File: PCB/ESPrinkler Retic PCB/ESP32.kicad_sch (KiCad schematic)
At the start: 2 parts, among them J3 Conn_01x19, J4 Conn_01x19

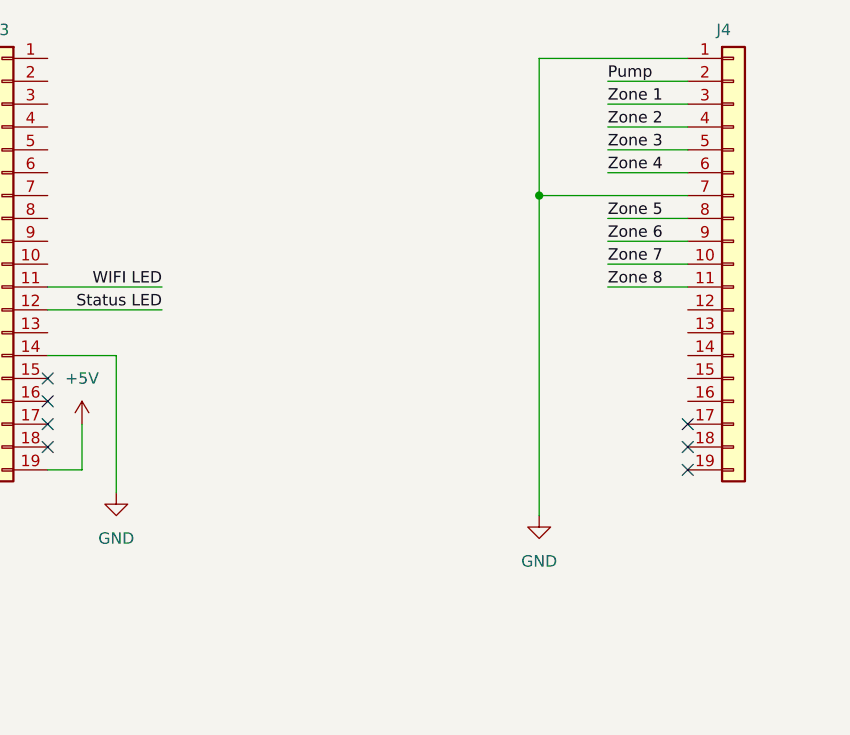
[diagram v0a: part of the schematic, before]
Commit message: Continue migrating PCB project to multi sheet design
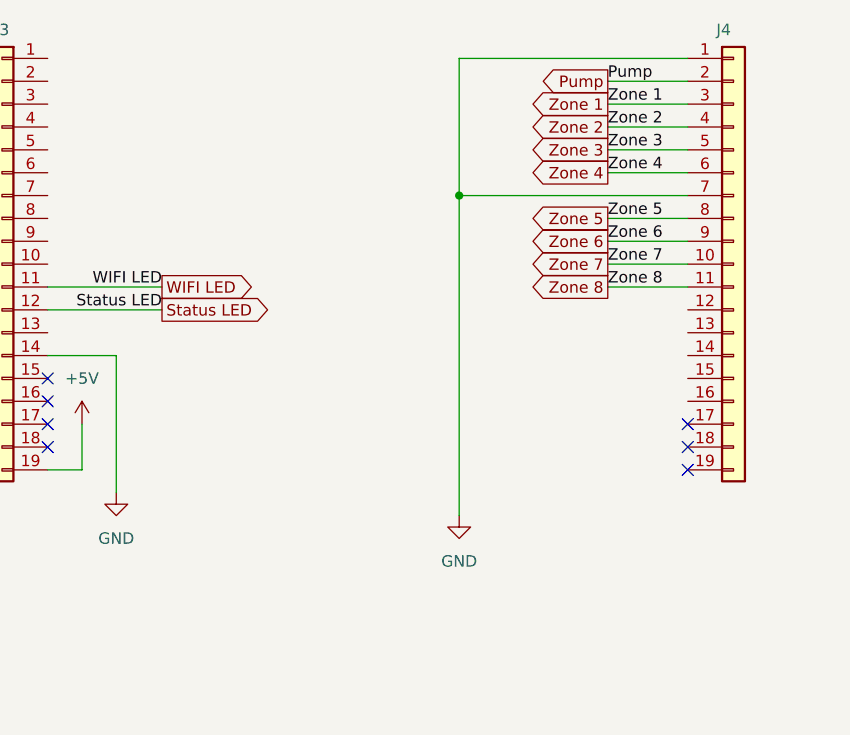
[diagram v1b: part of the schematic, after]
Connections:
- net Pump CTRL renamed Pump
- net Status LED CTRL renamed Status LED
- net WIFI LED CTRL renamed WIFI LED
- net Zone 1 CTRL renamed Zone 1
- net Zone 2 CTRL renamed Zone 2
- net Zone 3 CTRL renamed Zone 3
- net Zone 4 CTRL renamed Zone 4
- net Zone 5 CTRL renamed Zone 5
- net Zone 6 CTRL renamed Zone 6
- net Zone 7 CTRL renamed Zone 7
- net Zone 8 CTRL renamed Zone 8

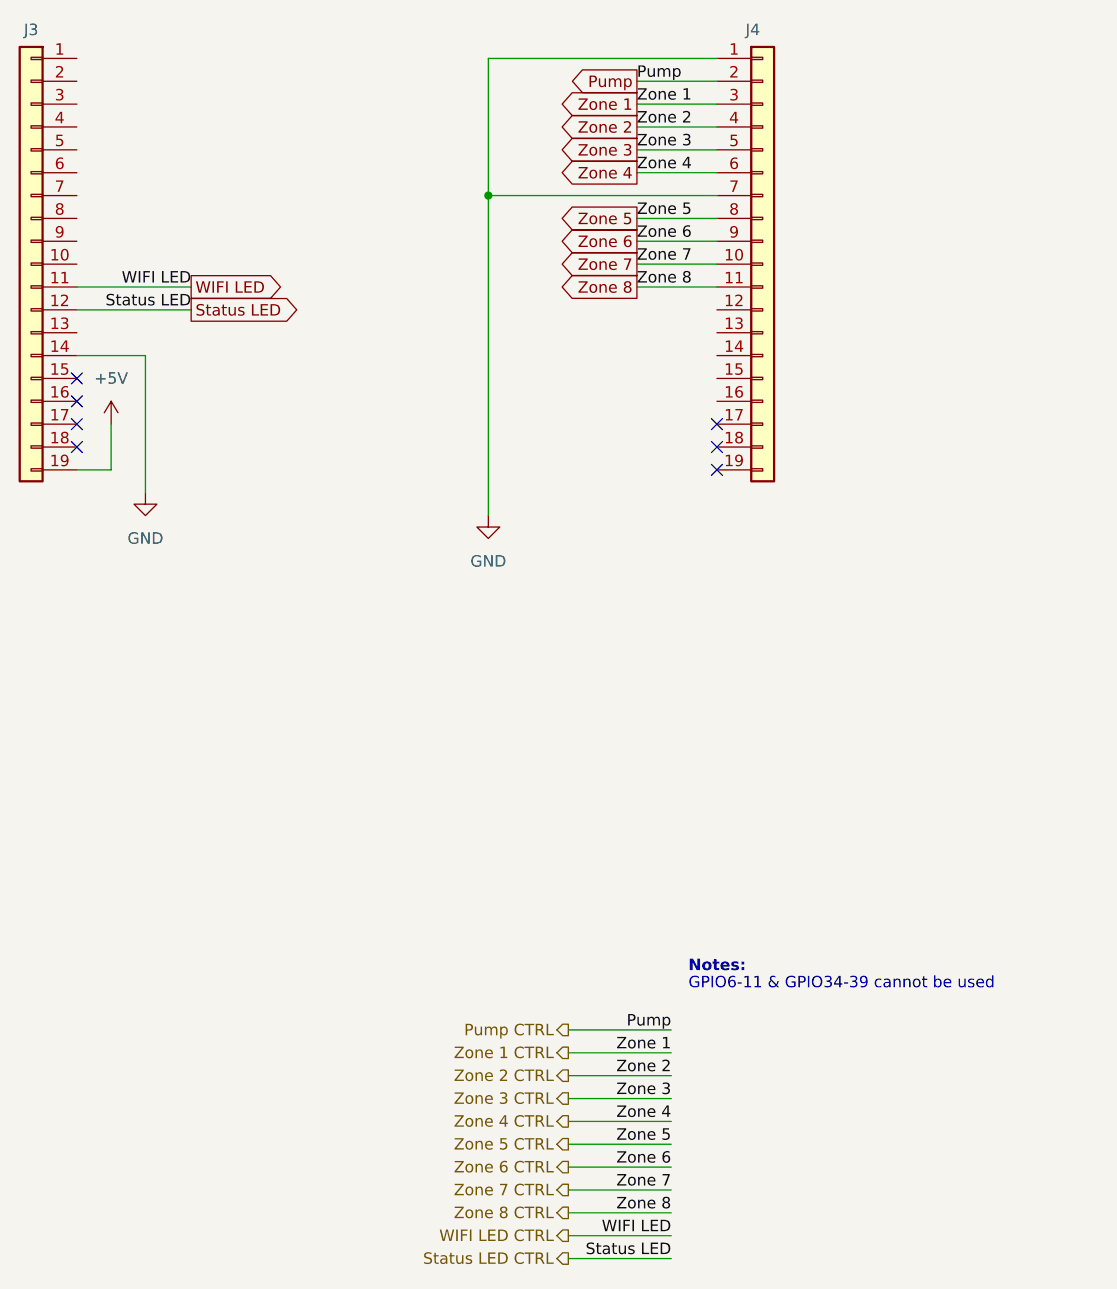
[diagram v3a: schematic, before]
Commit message: Initial schematic design completed
Finish initial schematic design and source all required components. DRC completed with only minor warnings (regarding net names, no worries). Move on to begin PCB design
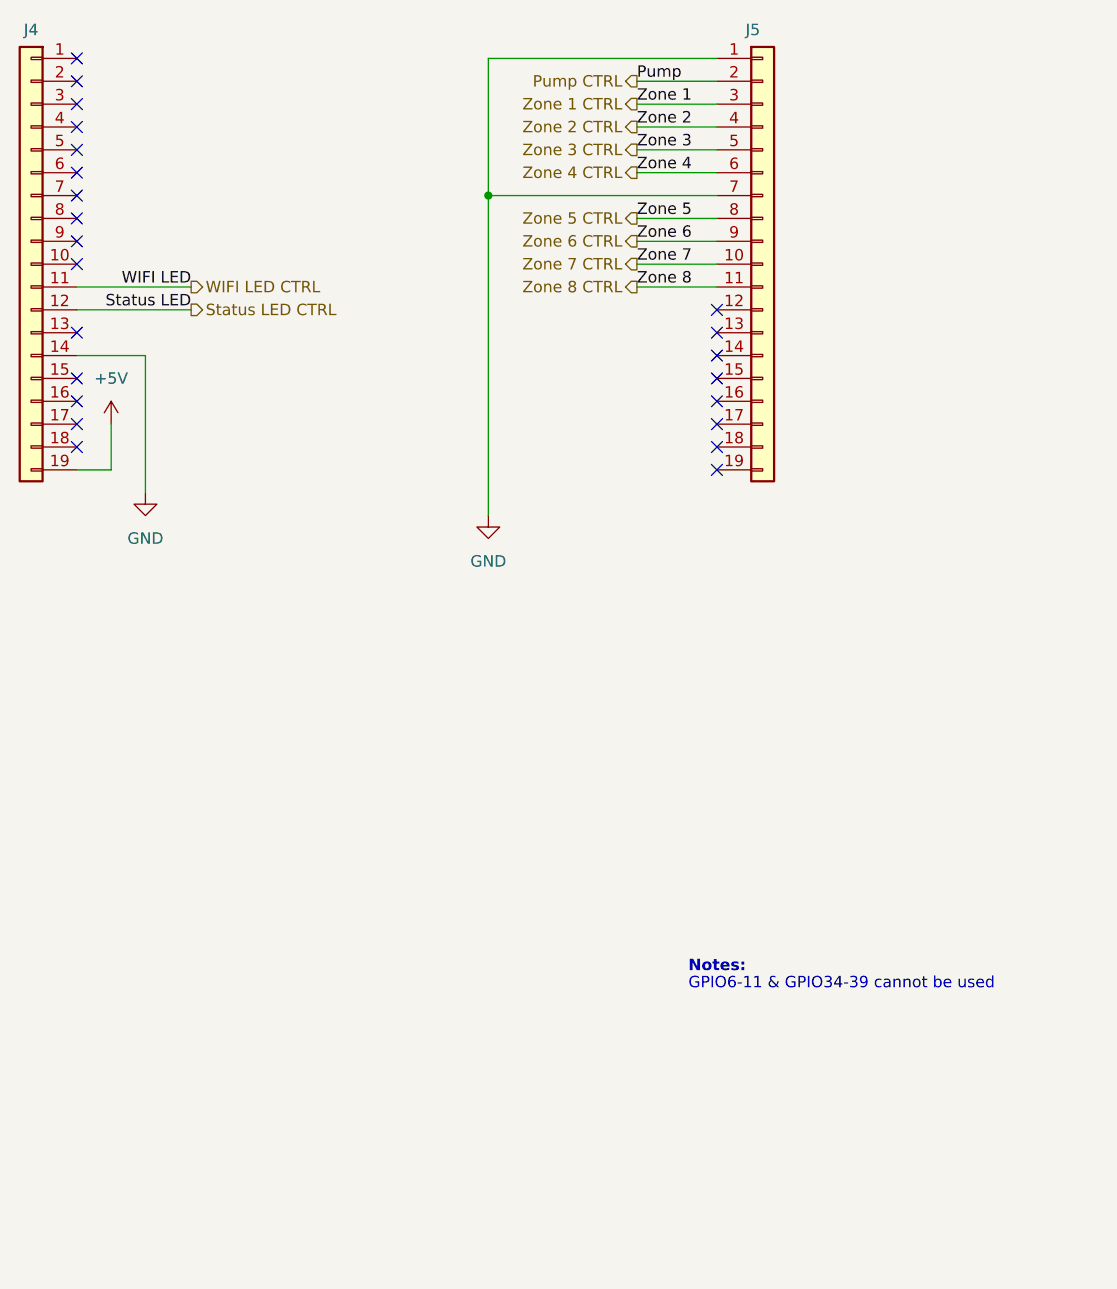
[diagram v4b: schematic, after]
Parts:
- J4: renamed from J3; footprint (none) -> Connector_PinSocket_2.54mm:PinSocket_1x19_P2.54mm_Vertical; Manufacturer (none) -> Shenzhen Kinghelm Elec; Manufacturer P/N (none) -> KH-2.54FH-1X19P-H8.5; Supplier (none) -> LCSC; Supplier P/N (none) -> C2932678
- J5: renamed from J4; footprint (none) -> Connector_PinSocket_2.54mm:PinSocket_1x19_P2.54mm_Vertical; Manufacturer (none) -> Shenzhen Kinghelm Elec; Manufacturer P/N (none) -> KH-2.54FH-1X19P-H8.5; Supplier (none) -> LCSC; Supplier P/N (none) -> C2932678
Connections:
- net Pump renamed Pump CTRL
- net Status LED renamed Status LED CTRL
- net WIFI LED renamed WIFI LED CTRL
- net Zone 1 renamed Zone 1 CTRL
- net Zone 2 renamed Zone 2 CTRL
- net Zone 3 renamed Zone 3 CTRL
- net Zone 4 renamed Zone 4 CTRL
- net Zone 5 renamed Zone 5 CTRL
- net Zone 6 renamed Zone 6 CTRL
- net Zone 7 renamed Zone 7 CTRL
- net Zone 8 renamed Zone 8 CTRL
- no-connect marks 7 -> 23

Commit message: Continue PCB design
Change footprint of triacs to include solder tab for securing package to PCB and heat dissipation.

Change footprint of optocoupler for better solder mask outlines and smaller pads.
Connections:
- net Pump CTRL: now also J5.11 (Pin_11); no longer J5.2 (Pin_2)
- net Zone 1 CTRL: now also J5.10 (Pin_10); no longer J5.3 (Pin_3)
- net Zone 2 CTRL: now also J5.9 (Pin_9); no longer J5.4 (Pin_4)
- net Zone 3 CTRL: now also J5.8 (Pin_8); no longer J5.5 (Pin_5)
- net Zone 5 CTRL: now also J5.5 (Pin_5); no longer J5.8 (Pin_8)
- net Zone 6 CTRL: now also J5.4 (Pin_4); no longer J5.9 (Pin_9)
- net Zone 7 CTRL: now also J5.3 (Pin_3); no longer J5.10 (Pin_10)
- net Zone 8 CTRL: now also J5.2 (Pin_2); no longer J5.11 (Pin_11)
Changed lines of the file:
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@@
 	)
 	(label "Pump"
-		(at 171.45 64.77 0)
+		(at 171.45 87.63 0)
 		(effects
 			(font
@@
 	)
 	(label "Zone 1"
-		(at 171.45 67.31 0)
+		(at 171.45 85.09 0)
 		(effects
 			(font
@@
 	)
 	(label "Zone 6"
-		(at 171.45 82.55 0)
+		(at 171.45 69.85 0)
 		(effects
 			(font
@@
 	)
 	(label "Zone 2"
-		(at 171.45 69.85 0)
+		(at 171.45 82.55 0)
 		(effects
 			(font
@@
 	)
 	(label "Zone 5"
+		(at 171.45 72.39 0)
+		(effects
+			(font
+				(size 1.27 1.27)
+			)
+			(justify left bottom)
+		)
+	)
+	(label "Zone 7"
+		(at 171.45 67.31 0)
+		(effects
+			(font
+				(size 1.27 1.27)
+			)
+			(justify left bottom)
+		)
+	)
+	(label "Zone 3"
 		(at 171.45 80.01 0)
 		(effects
@@
 		)
 	)
-	(label "Zone 7"
-		(at 171.45 85.09 0)
-		(effects
-			(font
-				(size 1.27 1.27)
-			)
-			(justify left bottom)
-		)
-	)
-	(label "Zone 3"
-		(at 171.45 72.39 0)
-		(effects
-			(font
-				(size 1.27 1.27)
-			)
-			(justify left bottom)
-		)
-	)
 	(label "Zone 8"
-		(at 171.45 87.63 0)
+		(at 171.45 64.77 0)
 		(effects
 			(font
@@
 	(hierarchical_label "Zone 1 CTRL"
 		(shape output)
+		(at 171.45 85.09 180)
+		(effects
+			(font
+				(size 1.27 1.27)
+			)
+			(justify right)
+		)
+	)
+	(hierarchical_label "Zone 4 CTRL"
+		(shape output)
+		(at 171.45 74.93 180)
+		(effects
+			(font
+				(size 1.27 1.27)
+			)
+			(justify right)
+		)
+	)
+	(hierarchical_label "Zone 2 CTRL"
+		(shape output)
+		(at 171.45 82.55 180)
+		(effects
+			(font
+				(size 1.27 1.27)
+			)
+			(justify right)
+		)
+	)
+	(hierarchical_label "Zone 3 CTRL"
+		(shape output)
+		(at 171.45 80.01 180)
+		(effects
+			(font
+				(size 1.27 1.27)
+			)
+			(justify right)
+		)
+	)
+	(hierarchical_label "Status LED CTRL"
+		(shape output)
+		(at 121.92 90.17 0)
+		(effects
+			(font
+				(size 1.27 1.27)
+			)
+			(justify left)
+		)
+	)
+	(hierarchical_label "Zone 6 CTRL"
+		(shape output)
+		(at 171.45 69.85 180)
+		(effects
+			(font
+				(size 1.27 1.27)
+			)
+			(justify right)
+		)
+	)
+	(hierarchical_label "WIFI LED CTRL"
+		(shape output)
+		(at 121.92 87.63 0)
+		(effects
+			(font
+				(size 1.27 1.27)
+			)
+			(justify left)
+		)
+	)
+	(hierarchical_label "Zone 5 CTRL"
+		(shape output)
+		(at 171.45 72.39 180)
+		(effects
+			(font
+				(size 1.27 1.27)
+			)
+			(justify right)
+		)
+	)
+	(hierarchical_label "Pump CTRL"
+		(shape output)
+		(at 171.45 87.63 180)
+		(effects
+			(font
+				(size 1.27 1.27)
+			)
+			(justify right)
+		)
+	)
+	(hierarchical_label "Zone 8 CTRL"
+		(shape output)
+		(at 171.45 64.77 180)
+		(effects
+			(font
+				(size 1.27 1.27)
+			)
+			(justify right)
+		)
+	)
+	(hierarchical_label "Zone 7 CTRL"
+		(shape output)
 		(at 171.45 67.31 180)
 		(effects
 			(font
-				(size 1.27 1.27)
-			)
-			(justify right)
-		)
-	)
-	(hierarchical_label "Zone 4 CTRL"
-		(shape output)
-		(at 171.45 74.93 180)
-		(effects
-			(font
-				(size 1.27 1.27)
-			)
-			(justify right)
-		)
-	)
-	(hierarchical_label "Zone 2 CTRL"
-		(shape output)
-		(at 171.45 69.85 180)
-		(effects
-			(font
-				(size 1.27 1.27)
-			)
-			(justify right)
-		)
-	)
-	(hierarchical_label "Zone 3 CTRL"
-		(shape output)
-		(at 171.45 72.39 180)
-		(effects
-			(font
-				(size 1.27 1.27)
-			)
-			(justify right)
-		)
-	)
-	(hierarchical_label "Status LED CTRL"
-		(shape output)
-		(at 121.92 90.17 0)
-		(effects
-			(font
-				(size 1.27 1.27)
-			)
-			(justify left)
-		)
-	)
-	(hierarchical_label "Zone 6 CTRL"
-		(shape output)
-		(at 171.45 82.55 180)
-		(effects
-			(font
-				(size 1.27 1.27)
-			)
-			(justify right)
-		)
-	)
-	(hierarchical_label "WIFI LED CTRL"
-		(shape output)
-		(at 121.92 87.63 0)
-		(effects
-			(font
-				(size 1.27 1.27)
-			)
-			(justify left)
-		)
-	)
-	(hierarchical_label "Zone 5 CTRL"
-		(shape output)
-		(at 171.45 80.01 180)
-		(effects
-			(font
-				(size 1.27 1.27)
-			)
-			(justify right)
-		)
-	)
-	(hierarchical_label "Pump CTRL"
-		(shape output)
-		(at 171.45 64.77 180)
-		(effects
-			(font
-				(size 1.27 1.27)
-			)
-			(justify right)
-		)
-	)
-	(hierarchical_label "Zone 8 CTRL"
-		(shape output)
-		(at 171.45 87.63 180)
-		(effects
-			(font
-				(size 1.27 1.27)
-			)
-			(justify right)
-		)
-	)
-	(hierarchical_label "Zone 7 CTRL"
-		(shape output)
-		(at 171.45 85.09 180)
-		(effects
-			(font

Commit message: Modify SCH
Remote ~ from datasheet section and spelling mistake on parts list.

Swap status and wifi led control GPIOs for easier PCB traces
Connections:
- net Status LED CTRL: now also J4.11 (Pin_11); no longer J4.12 (Pin_12)
- net WIFI LED CTRL: now also J4.12 (Pin_12); no longer J4.11 (Pin_11)
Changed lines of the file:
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@@
 	)
 	(label "WIFI LED"
-		(at 121.92 87.63 180)
+		(at 121.92 90.17 180)
 		(effects
 			(font
@@
 	)
 	(label "Status LED"
-		(at 121.92 90.17 180)
+		(at 121.92 87.63 180)
 		(effects
 			(font
@@
 	(hierarchical_label "Status LED CTRL"
 		(shape output)
-		(at 121.92 90.17 0)
+		(at 121.92 87.63 0)
 		(effects
 			(font
@@
 	(hierarchical_label "WIFI LED CTRL"
 		(shape output)
-		(at 121.92 87.63 0)
+		(at 121.92 90.17 0)
 		(effects
 			(font

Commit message: Update Schematics
For all, update title block information.

Power IO:
- Change PTC fuse footprint reference
- Add part info for J1

Control Outputs:
- Add notes and box areas of schematic for clarity
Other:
- title: (none) -> ESPrinkler Retic Controller
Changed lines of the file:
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@@
 	(generator_version "9.0")
 	(paper "A4")
+	(title_block
+		(title "ESPrinkler Retic Controller")
+		(date "2025-06-01")
+		(rev "1.0")
+	)
 	(text "GPIO6-11 & GPIO34-39 cannot be used"
 		(exclude_from_sim no)
